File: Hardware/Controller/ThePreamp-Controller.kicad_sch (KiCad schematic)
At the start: 30 parts, among them J1 B1 Relays, J10 I2C (FUTURE USE), J11 ROTARY ENC & SWITCH 1, J12 ROTARY ENC & SWITCH 2, J13 IR RECV, J14 12V, J15 8V, J2 PWR AMP L 12V TRIGGER, J3 PWR AMP L SWITCH, J4 PWR AMP R 12V TRIGGER, J5 PWR AMP R SWITCH, J6 PWR AMP TEMP NTC L, J7 PWR AMP TEMP NTC R, J8 MUSES 72320 (SPI), J9 I2C DISPLAY (OLED/LCD), U1 AGQ20T03, U2 AGQ20T03, U3 ULN2803ADWR, U4 MCP23008-E_SO, U5 24C02C_SN, U6 ESP32-DEVKIT-V1

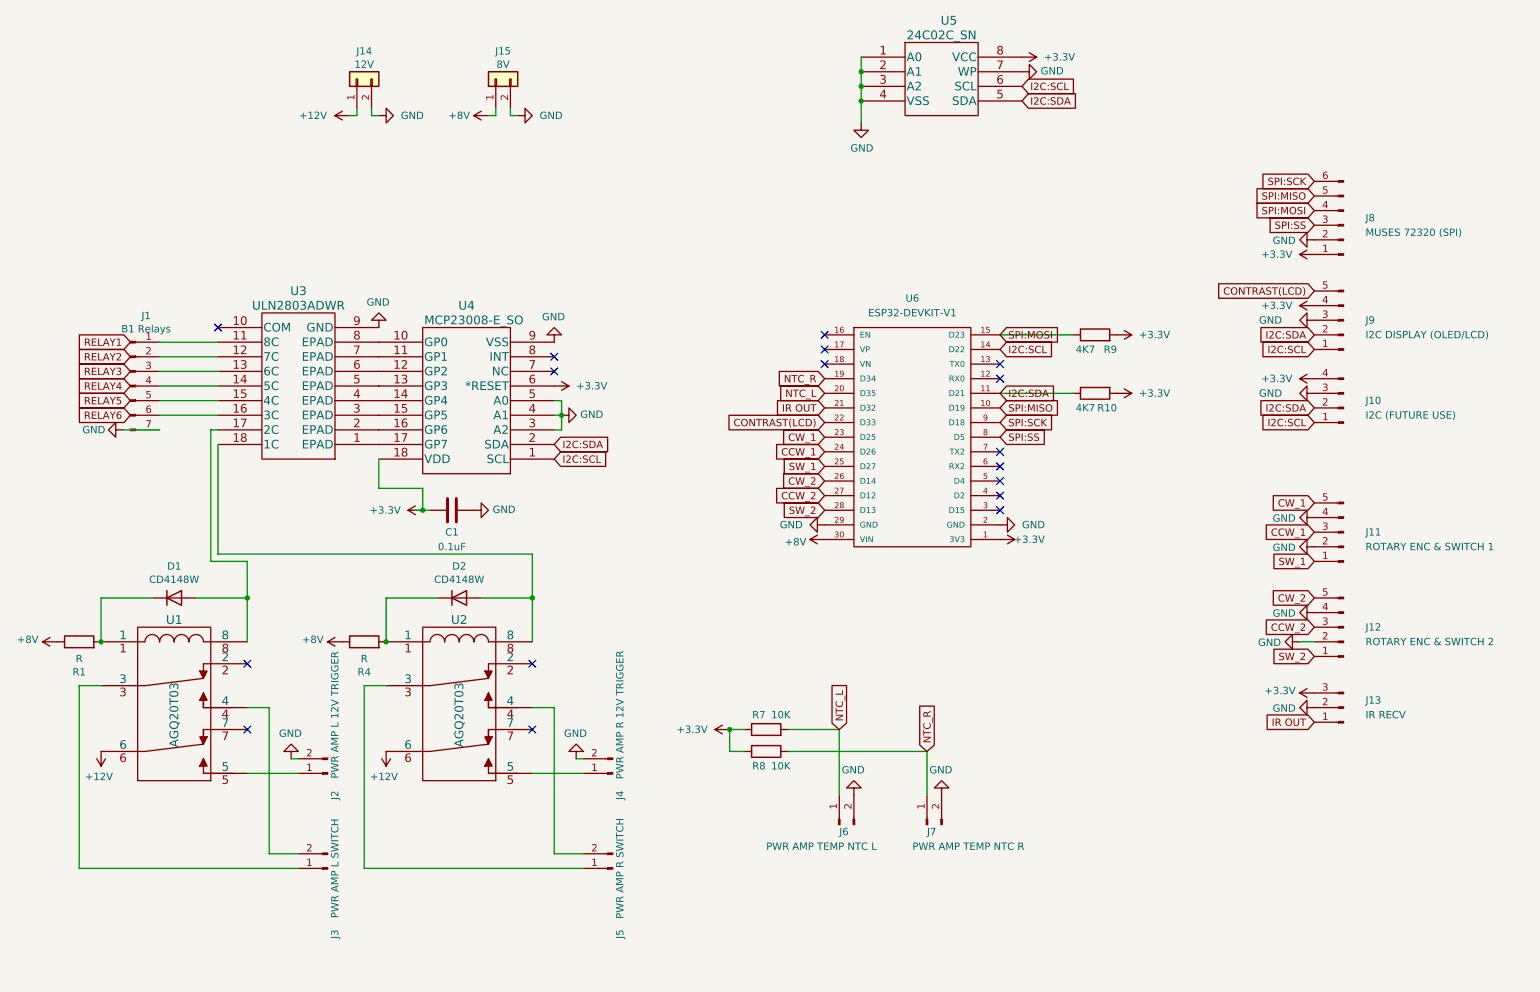
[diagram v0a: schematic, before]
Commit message: Controller pcb dimensions added
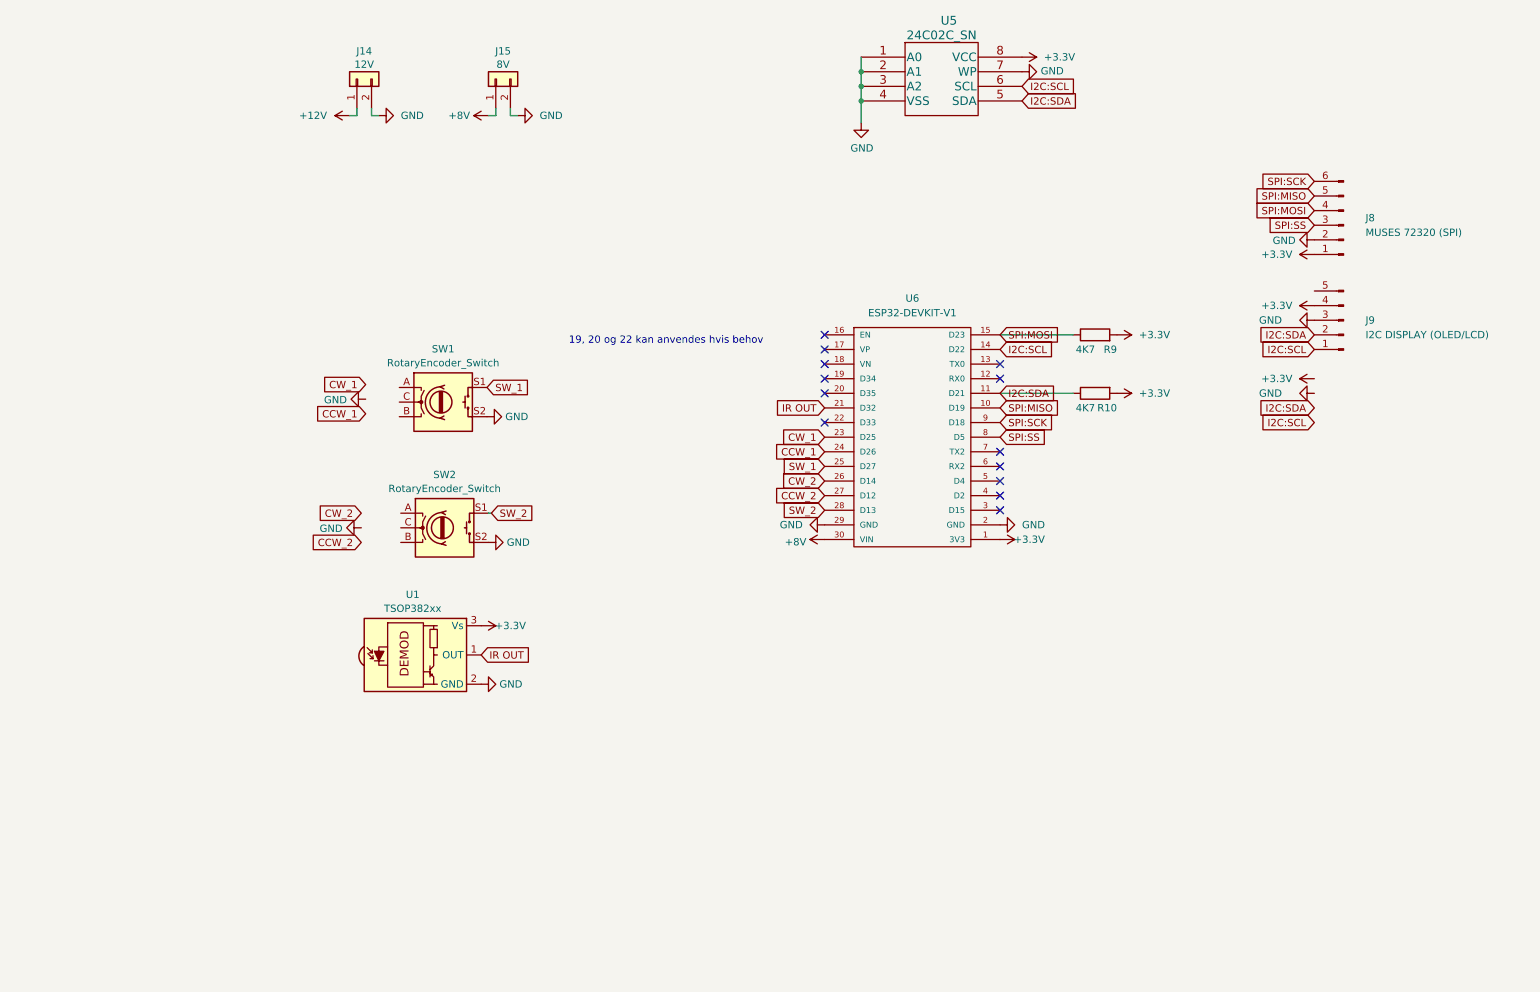
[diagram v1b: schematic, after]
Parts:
- removed C1: 0.1uF, Capacitor_SMD:C_0805_2012Metric_Pad1.15x1.40mm_HandSolder, symbol Device:C
- removed D1, D2: CD4148W, Diode_SMD:D_0805_2012Metric, symbol Diode:CD4148W
- removed J1: B1 Relays, Connector_JST:JST_XH_B7B-XH-A_1x07_P2.50mm_Vertical, symbol Connector:Conn_01x07_Male
- removed J10: I2C (FUTURE USE), Connector_JST:JST_XH_B4B-XH-A_1x04_P2.50mm_Vertical, symbol Connector:Conn_01x04_Male
- removed J11: ROTARY ENC & SWITCH 1, Connector_JST:JST_XH_B5B-XH-A_1x05_P2.50mm_Vertical, symbol Connector:Conn_01x05_Male
- removed J12: ROTARY ENC & SWITCH 2, Connector_JST:JST_XH_B5B-XH-A_1x05_P2.50mm_Vertical, symbol Connector:Conn_01x05_Male
- removed J13: IR RECV, Connector_JST:JST_XH_B3B-XH-A_1x03_P2.50mm_Vertical, symbol Connector:Conn_01x03_Male
- removed J2: PWR AMP L 12V TRIGGER, Connector_JST:JST_XH_B2B-XH-A_1x02_P2.50mm_Vertical, symbol Connector:Conn_01x02_Male
- removed J3: PWR AMP L SWITCH, Connector_JST:JST_XH_B2B-XH-A_1x02_P2.50mm_Vertical, symbol Connector:Conn_01x02_Male
- removed J4: PWR AMP R 12V TRIGGER, Connector_JST:JST_XH_B2B-XH-A_1x02_P2.50mm_Vertical, symbol Connector:Conn_01x02_Male
- removed J5: PWR AMP R SWITCH, Connector_JST:JST_XH_B2B-XH-A_1x02_P2.50mm_Vertical, symbol Connector:Conn_01x02_Male
- removed J6: PWR AMP TEMP NTC L, Connector_JST:JST_XH_B2B-XH-A_1x02_P2.50mm_Vertical, symbol Connector:Conn_01x02_Male
- removed J7: PWR AMP TEMP NTC R, Connector_JST:JST_XH_B2B-XH-A_1x02_P2.50mm_Vertical, symbol Connector:Conn_01x02_Male
- removed R1, R4: R, Resistor_THT:R_Axial_DIN0207_L6.3mm_D2.5mm_P10.16mm_Horizontal, symbol Device:R
- removed R7, R8: 10K, Resistor_SMD:R_0805_2012Metric_Pad1.15x1.40mm_HandSolder, symbol Device:R
- removed U1, U2: AGQ20T03, AGQ20T03_footprint:AGQ20012, symbol Mezmerize_B1_Controller-rescue:AGQ20012-2019-11-30_08-42-06
- removed U3: ULN2803ADWR, ULN2803:ULN2803ADWR, symbol Mezmerize_B1_Controller-rescue:ULN2803ADWR-2019-12-07_08-18-10
- removed U4: MCP23008-E_SO, MCP23008:MCP23008-E&slash_SO, symbol Mezmerize_B1_Controller-rescue:MCP23008-E_SO-2019-12-07_08-25-49
- added SW1, SW2: RotaryEncoder_Switch, Rotary_Encoder:RotaryEncoder_Alps_EC11E-Switch_Vertical_H20mm, symbol Device:RotaryEncoder_Switch
- added U1: TSOP382xx, OptoDevice:Vishay_MINICAST-3Pin, symbol Interface_Optical:TSOP382xx
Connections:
- net +3V3: now also U1.3 (Vs)
- net GND: now also SW1.S2, SW2.S2, U1.2 (GND)
- net IR OUT: now also U1.1 (OUT)
- net SW_1: now also SW1.S1
- net SW_2: now also SW2.S1
- net CONTRAST(LCD): no longer names the net of J9.5 (Pin_5)
- net CONTRAST(LCD): no longer U6.22 (D33)
- net NTC_L: no longer names the net of U6.20 (D35)
- net NTC_R: no longer names the net of U6.19 (D34)
- no-connect marks 17 -> 13
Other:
- note added: "19, 20 og 22 kan anvendes hvis behov"

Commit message: Displays changed to SPI
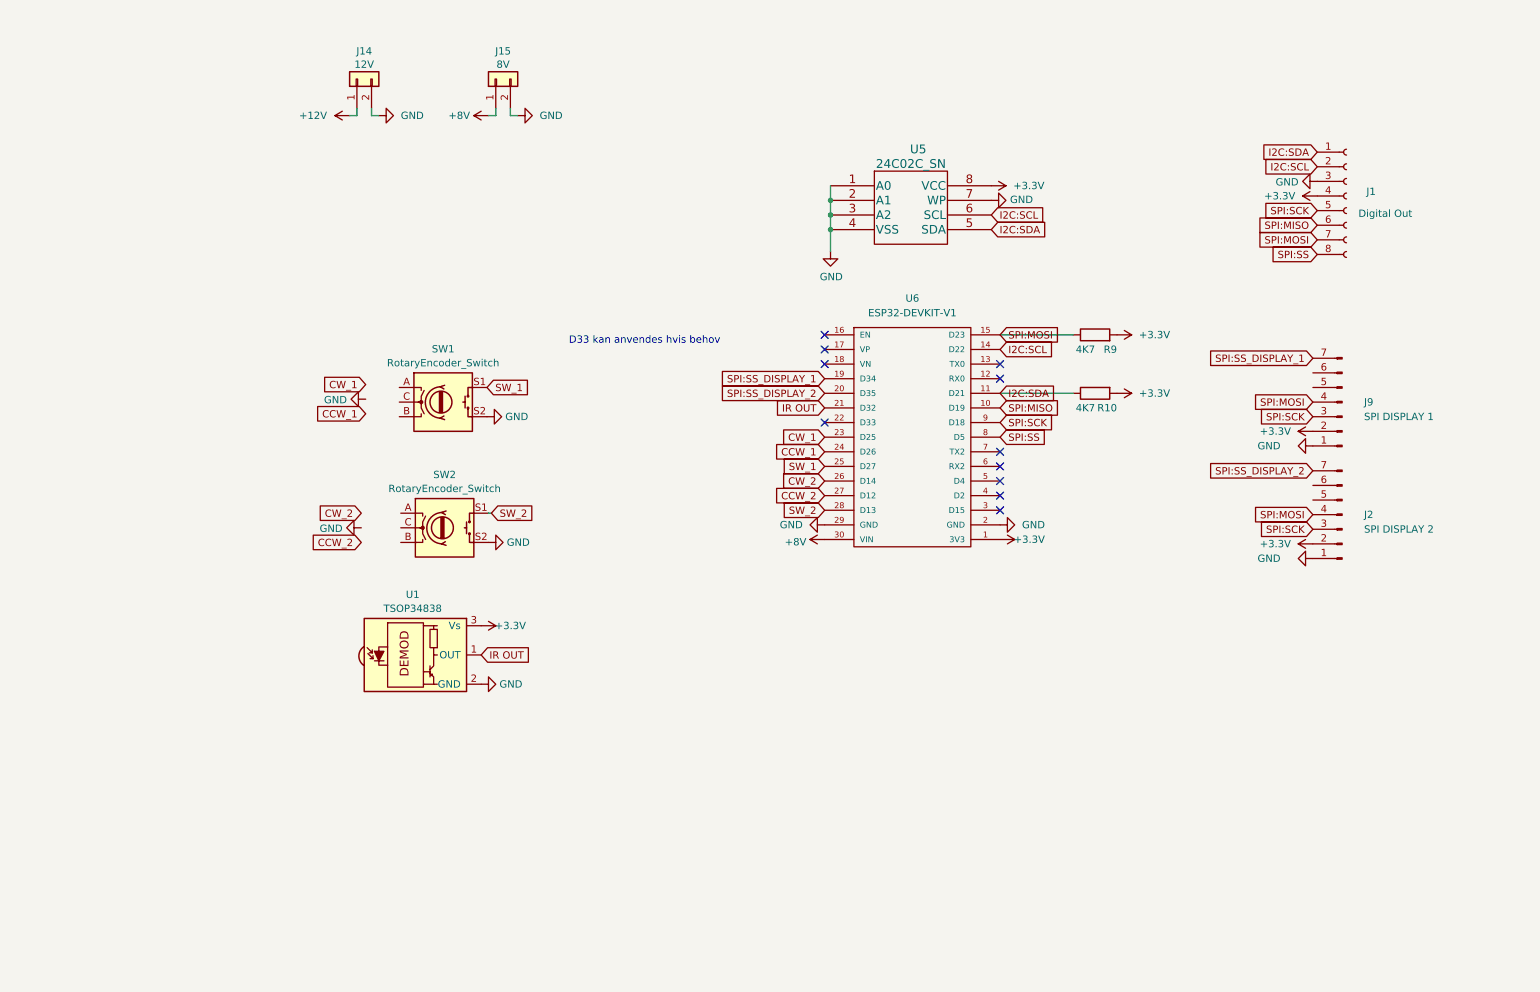
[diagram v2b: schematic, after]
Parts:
- removed J8: MUSES 72320 (SPI), Connector_JST:JST_XH_B6B-XH-A_1x06_P2.50mm_Vertical, symbol Connector:Conn_01x06_Male
- added J1: Digital Out, Connector_JST:JST_XH_B8B-XH-A_1x08_P2.50mm_Vertical, symbol Connector:Conn_01x08_Female
- added J2: SPI DISPLAY 2, Connector_PinHeader_2.54mm:PinHeader_1x07_P2.54mm_Vertical, symbol Connector:Conn_01x07_Pin
- J9: value I2C DISPLAY (OLED/LCD) -> SPI DISPLAY 1; footprint Connector_JST:JST_XH_B5B-XH-A_1x05_P2.50mm_Vertical -> Connector_PinHeader_2.54mm:PinHeader_1x07_P2.54mm_Vertical; symbol Connector:Conn_01x05_Male -> Connector:Conn_01x07_Pin
- U1: value TSOP382xx -> TSOP34838; footprint OptoDevice:Vishay_MINICAST-3Pin -> OptoDevice:Vishay_MOLD-3Pin; symbol Interface_Optical:TSOP382xx -> Interface_Optical:TSOP348xx
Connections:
- net +3V3: now also J9.2 (Pin_2), J1.4 (Pin_4), J2.2 (Pin_2); no longer J9.4 (Pin_4)
- net GND: now also J9.1 (Pin_1), J1.3 (Pin_3), J2.1 (Pin_1); no longer J9.3 (Pin_3)
- net I2C:SCL: now also J1.2 (Pin_2); no longer J9.1 (Pin_1)
- net I2C:SDA: now also J1.1 (Pin_1); no longer J9.2 (Pin_2)
- net SPI:MISO: now also J1.6 (Pin_6)
- net SPI:MOSI: now also J9.4 (Pin_4), J1.7 (Pin_7), J2.4 (Pin_4)
- net SPI:SCK: now also J9.3 (Pin_3), J1.5 (Pin_5), J2.3 (Pin_3)
- net SPI:SS: now also J1.8 (Pin_8)
- net SPI:SS_DISPLAY_1: now reaches U6.19 (D34)
- net SPI:SS_DISPLAY_1: now also J9.7 (Pin_7)
- net SPI:SS_DISPLAY_2: now reaches U6.20 (D35)
- net SPI:SS_DISPLAY_2: now also J2.7 (Pin_7)
- no-connect marks 13 -> 11
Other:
- note added: "D33 kan anvendes hvis behov"
- note removed: "19, 20 og 22 kan anvendes hvis behov"
- moved on the sheet: U5

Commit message: Test code for two displays
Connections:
- net IR RECV: now reaches U6.3 (D15)
- net IR RECV: now also U1.1 (OUT)
- net IR OUT: no longer names the net of U6.21 (D32)
- net IR OUT: no longer U1.1 (OUT)
- no-connect marks 11 -> 9
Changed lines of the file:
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@@
   (no_connect (at 187.96 78.74))
   (no_connect (at 187.96 81.28))
-  (no_connect (at 157.48 88.9))
   (no_connect (at 187.96 99.06))
-  (no_connect (at 187.96 104.14))
   (no_connect (at 187.96 101.6))
   (no_connect (at 157.48 78.74))
@@
     )
   )
-  (global_label "IR OUT" (shape input) (at 157.48 86.36 180) (fields_autoplaced)
-    (effects (font (size 1.27 1.27)) (justify right))
-    (property "Intersheetrefs" "${INTERSHEET_REFS}" (at 148.6848 86.2806 0)
-      (effects (font (size 1.27 1.27)) (justify right) hide)
+  (global_label "IR RECV" (shape input) (at 187.96 104.14 0) (fields_autoplaced)
+    (effects (font (size 1.27 1.27)) (justify left))
+    (property "Intersheetrefs" "${INTERSHEET_REFS}" (at 197.911 104.14 0)
+      (effects (font (size 1.27 1.27)) (justify left) hide)
     )
   )
@@
     )
   )
-  (global_label "IR OUT" (shape input) (at 97.79 129.286 0) (fields_autoplaced)
-    (effects (font (size 1.27 1.27)) (justify left))
-    (property "Intersheetrefs" "${INTERSHEET_REFS}" (at 106.592 129.286 0)
-      (effects (font (size 1.27 1.27)) (justify left) hide)
-    )
+  (global_label "IR RECV" (shape input) (at 97.79 129.286 0) (fields_autoplaced)
+    (effects (font (size 1.27 1.27)) (justify left))
+    (property "Intersheetrefs" "${INTERSHEET_REFS}" (at 107.741 129.286 0)
+      (effects (font (size 1.27 1.27)) (justify left) hide)
+    )
